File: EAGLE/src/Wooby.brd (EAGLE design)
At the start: 95 x 37 mm, 18 parts, among them J2 691210910002, J5 691210910002, U1 GY-521MPU6050

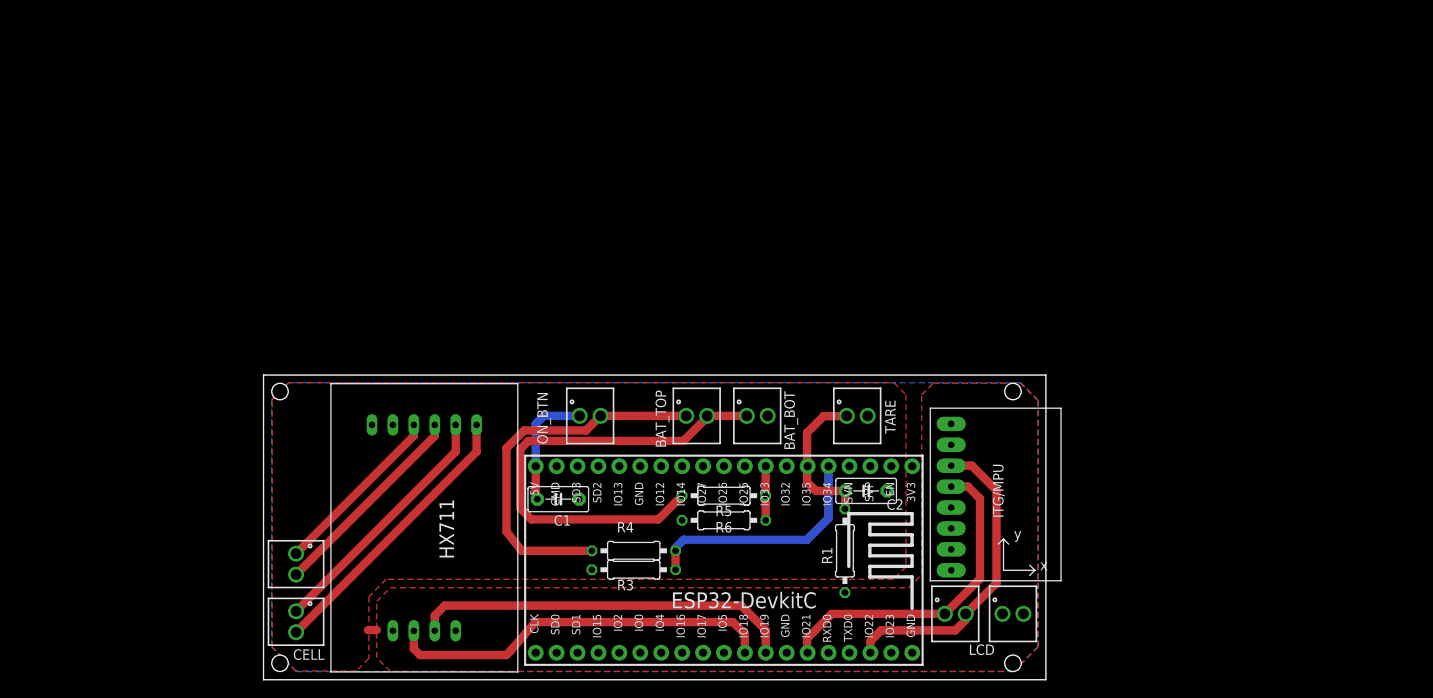
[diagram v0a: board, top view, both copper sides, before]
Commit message: EagleV2
With some improvements since the first V" printed version, but still with some improvements to be performed
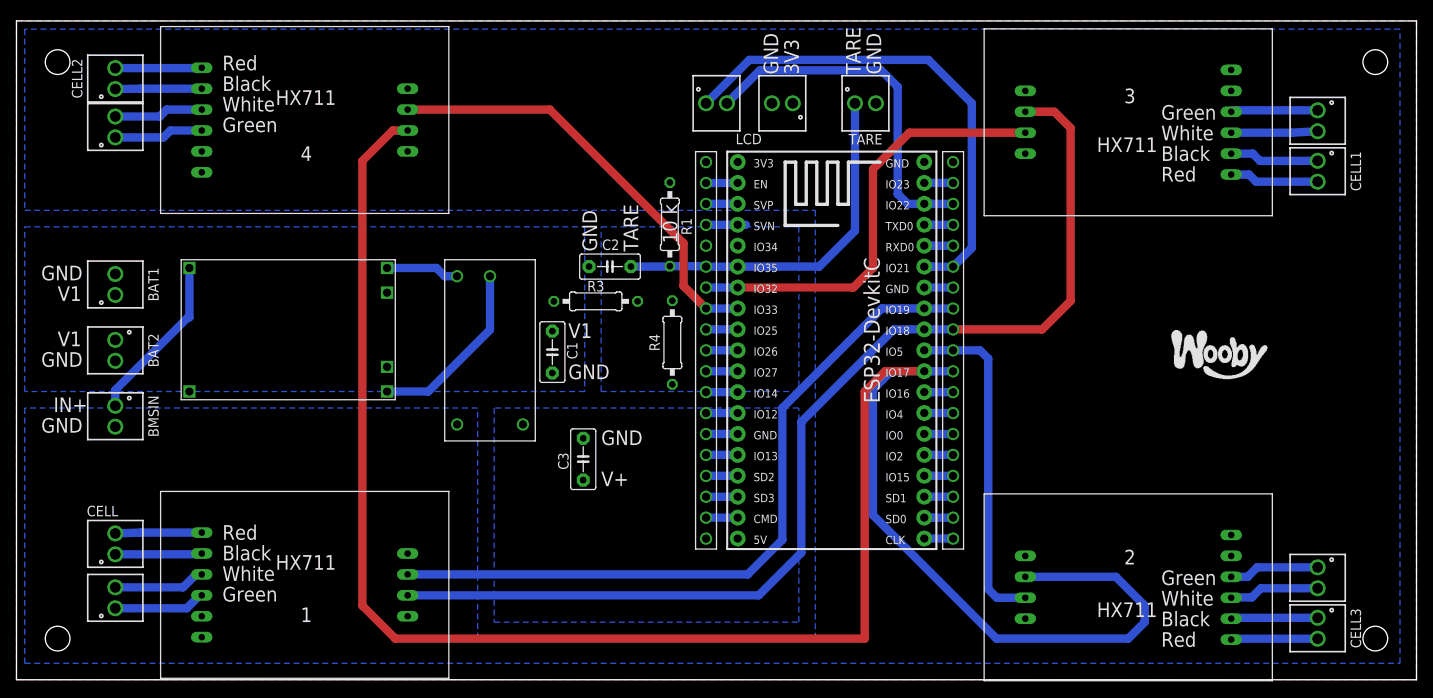
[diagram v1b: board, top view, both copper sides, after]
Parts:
- removed BAT_BOT, BAT_TOP, ON_BTN: 691210910002, 691210910002:691210910002
- removed R5, R6: (no value), rcl:0207/10
- removed U1: GY-521MPU6050, MPU-6050:GY-521
- added BAT1, BAT2, BMSIN, CELL1, CELL2, CELL3, J1, J3, J4: 691210910002, 691210910002:691210910002
- added C3: (no value), capacitor-wima:C5B3
- added SM2, SM3, SM4: (no value), hx711:HX711
- added SUC5V8V: STEPUPCONVERTOR5V8V, stepUpConverto5V8V:STEPUPCONVERTO5V8V
- added U$1: BMS, BMS:BMS
- added U$2, U$3: READER, READER:READER
- moved J2 68.4 mm to (85.0, 70.0)
- moved LCD 68.0 mm to (93.0, 70.0), turned to 180 degrees
- moved R1 45.0 mm to (79.3, 55.3), turned to 90 degrees
- moved C2 41.3 mm to (72.1, 50.2), turned to 180 degrees
- moved TARE 38.0 mm to (103.1, 70.0)
- moved R3 30.6 mm to (70.3, 46.0)
- moved ESP32-DEVKITC 28.7 mm to (99.0, 40.0), turned to 270 degrees
- moved R4 28.0 mm to (79.6, 41.0), turned to 90 degrees
- moved CELL 23.9 mm to (12.0, 16.5), turned to 90 degrees
- moved J5 22.3 mm to (12.0, 9.95), turned to 90 degrees
- moved C1 17.9 mm to (65.1, 39.8), turned to 270 degrees
- moved SM1 16.1 mm to (35.0, 11.5), turned to 0 degrees
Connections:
- removed net BAT_DOWN: ESP32-DEVKITC.8, R5.2, R6.2
- removed net BOTH_BAT: ESP32-DEVKITC.5, R3.1, R4.2
- removed net V2: BAT_TOP.1, ON_BTN.2, R3.2
- new net BATS: ESP32-DEVKITC.5, R3.1, R4.2, U$2.P5
- new net N$11: ESP32-DEVKITC.8, SM3.D1, U$2.P8
- new net N$12: ESP32-DEVKITC.29, SM4.D1, U$3.P10
- new net N$13: CELL3.2, SM4.A0
- new net N$14: CELL3.1, SM4.A1
- new net N$15: J4.2, SM4.A2
- new net N$16: J4.1, SM4.A3
- new net N$17: CELL2.2, SM3.A0
- new net N$18: CELL2.1, SM3.A1
- new net N$19: J3.2, SM3.A2
- new net N$20: J3.1, SM3.A3
- new net N$21: CELL1.2, SM2.A0
- new net N$22: CELL1.1, SM2.A1
- new net N$23: J1.2, SM2.A2
- new net N$24: J1.1, SM2.A3
- new net N$25: SUC5V8V.IN-, U$1.OUT-
- new net N$26: SUC5V8V.IN+, U$1.OUT+
- new net N$27: BMSIN.1, U$1.IN+
- new net N$28: ESP32-DEVKITC.18, U$2.P18
- new net N$29: ESP32-DEVKITC.17, U$2.P17
- new net N$30: ESP32-DEVKITC.16, U$2.P16
- new net N$31: ESP32-DEVKITC.15, U$2.P15
- new net N$32: ESP32-DEVKITC.14, U$2.P14
- new net N$33: ESP32-DEVKITC.13, U$2.P13
- new net N$34: ESP32-DEVKITC.12, U$2.P12
- new net N$35: ESP32-DEVKITC.11, U$2.P11
- new net N$36: ESP32-DEVKITC.10, U$2.P10
- new net N$37: ESP32-DEVKITC.9, U$2.P9
- new net N$38: ESP32-DEVKITC.4, U$2.P4
- new net N$39: ESP32-DEVKITC.3, U$2.P3
- new net N$40: ESP32-DEVKITC.2, U$2.P2
- new net N$41: ESP32-DEVKITC.20, U$3.P19
- new net N$42: ESP32-DEVKITC.21, U$3.P18
- new net N$43: ESP32-DEVKITC.22, U$3.P17
- new net N$44: ESP32-DEVKITC.23, U$3.P16
- new net N$45: ESP32-DEVKITC.24, U$3.P15
- new net N$46: ESP32-DEVKITC.25, U$3.P14
- new net N$47: ESP32-DEVKITC.26, U$3.P13
- new net N$48: ESP32-DEVKITC.27, U$3.P12
- new net N$49: ESP32-DEVKITC.32, U$3.P7
- new net N$5: ESP32-DEVKITC.7, SM2.D1, U$2.P7
- new net N$50: ESP32-DEVKITC.34, U$3.P5
- new net N$51: ESP32-DEVKITC.35, U$3.P4
- new net N$53: ESP32-DEVKITC.37, U$3.P2
- new net N$8: ESP32-DEVKITC.28, SM3.D2, SM4.D2, U$3.P11
- net +3V3: now also SM2.D3, SM3.D3, SM4.D3, U$2.P1; no longer U1.VCC
- net GND: now also BAT1.2, BAT2.2, BMSIN.2, C3.2, SM2.D0, SM3.D0, SM4.D0, SUC5V8V.OUT-, U$1.B-, U$1.IN-, U$3.P1; no longer BAT_BOT.2, R6.1, U1.GND
- net N$10: now also SM2.D2, U$3.P9
- net N$6: now also U$3.P3; no longer U1.SCL
- net N$7: now also U$3.P6; no longer U1.SDA
- net N$9: now also U$3.P8
- net TARE: now also U$2.P6
- net V+: now also C3.1, SUC5V8V.OUT+, U$2.P19; no longer C1.1, ON_BTN.1
- net V1: now also BAT1.1, BAT2.1, C1.1, R3.2, U$1.B+; no longer BAT_BOT.1, BAT_TOP.2, R5.1
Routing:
- net N$8: track 0.00 -> 245.8 mm
- net N$10: track 47.4 -> 131.9 mm
- net V1: track 57.8 -> 0.00 mm
- net N$5: track 0.00 -> 53.6 mm
- net N$11: track 0.00 -> 53.2 mm
- net V2: track 45.1 -> 0.00 mm
- net N$9: track 46.5 -> 89.0 mm
- net N$12: track 0.00 -> 41.1 mm
- net BOTH_BAT: track 29.1 -> 0.00 mm
- net TARE: track 19.0 -> 44.6 mm
- net N$2: track 34.3 -> 10.5 mm
- net N$25: track 0.00 -> 22.1 mm
- net N$7: track 39.6 -> 60.9 mm
- net N$27: track 0.00 -> 20.6 mm
- net N$1: track 30.7 -> 10.5 mm
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- added copper zone on layer 16, net BATS
- added copper zone on layer 16, net V+
- added copper zone on layer 16, net V1
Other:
- board size 95 x 37 mm -> 170 x 80 mm
- board text added: "1"
- board text added: "10 k"
- board text added: "2"
- board text added: "3"
- board text added: "3V3"
- board text added: "4"
- board text added: "Black"
- board text added: "GND"
- board text added: "Green"
- board text added: "IN+"
- board text added: "Red"
- board text added: "TARE"
- board text added: "V+"
- board text added: "V1"
- board text added: "White"

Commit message: ON_BTN insertion on circuit and board
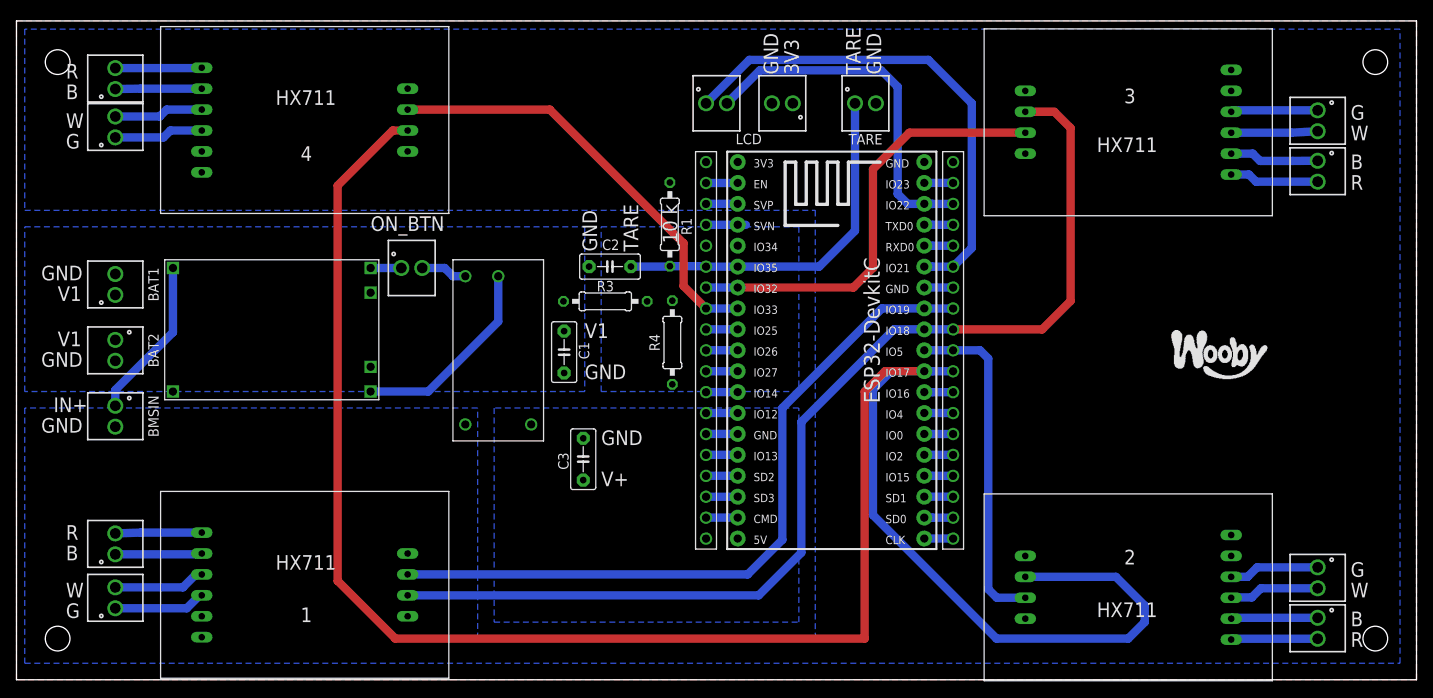
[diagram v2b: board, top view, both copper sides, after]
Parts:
- added ON_BTN: 691210910002, 691210910002:691210910002
- moved U$1 2.00 mm to (18.0, 51.0)
- moved C1 1.43 mm to (66.5, 39.8)
- moved R3 1.16 mm to (71.5, 46.0)
- moved SUC5V8V 1.00 mm to (64.0, 51.0)
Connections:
- new net N$52: ON_BTN.2, SUC5V8V.IN+
- net N$26: now also ON_BTN.1; no longer SUC5V8V.IN+
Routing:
- net N$52: track 0.00 -> 5.64 mm
- net N$26: track 8.91 -> 3.73 mm
- net N$8: track 245.8 -> 248.3 mm
- net N$25: track 22.1 -> 24.5 mm
- net N$27: track 20.6 -> 19.6 mm
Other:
- board text added: "B"
- board text added: "G"
- board text added: "ON_BTN"
- board text added: "R"
- board text added: "W"
- board text removed: "Black"
- board text removed: "Green"
- board text removed: "Red"
- board text removed: "White"
